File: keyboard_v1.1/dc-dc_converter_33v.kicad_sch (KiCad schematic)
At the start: 14 parts, among them Q2 AO3400A, U3 max1771esa+T

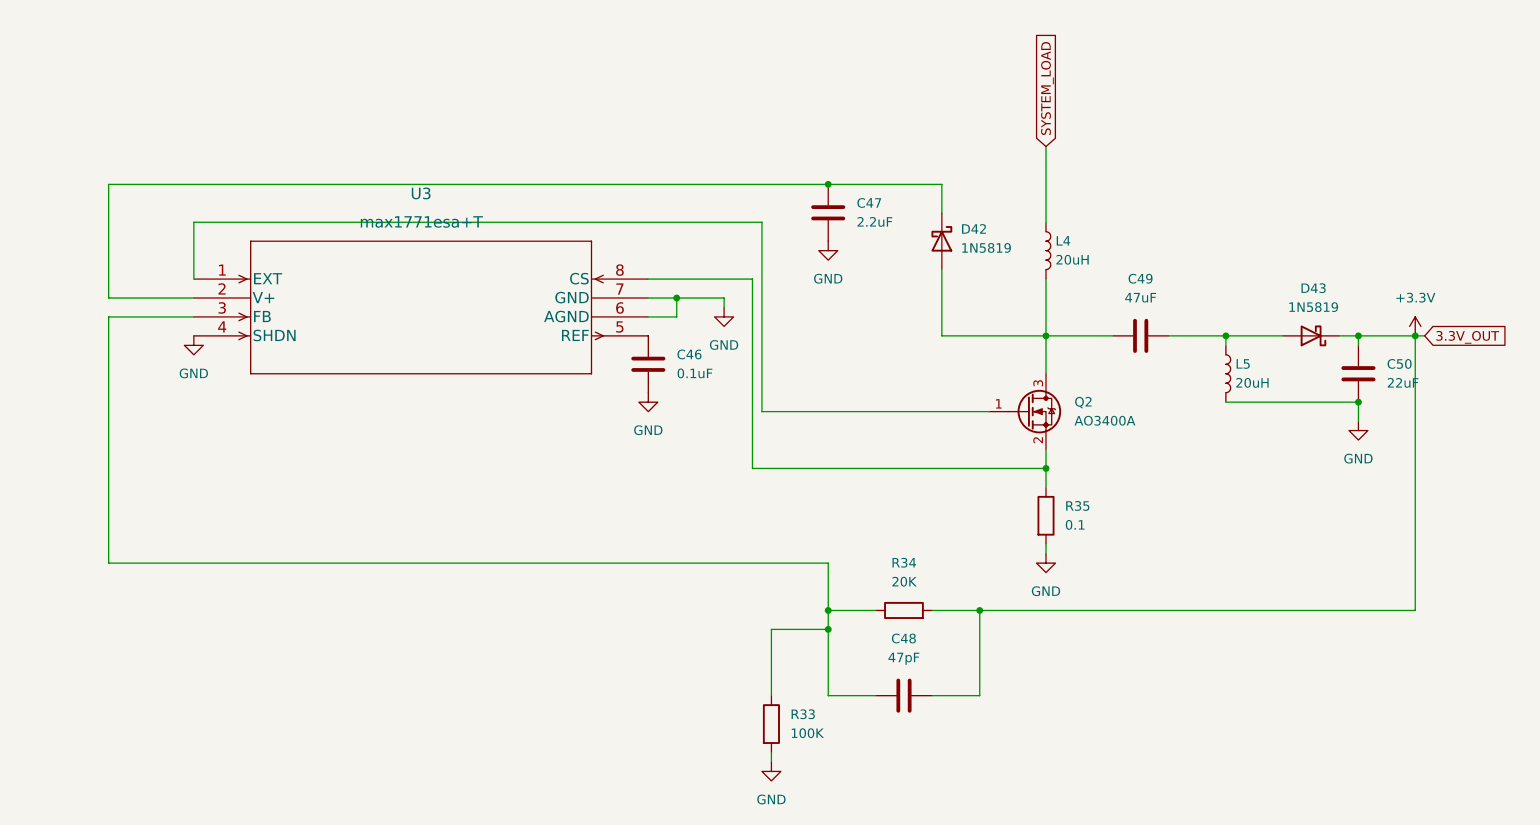
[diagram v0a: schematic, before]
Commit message: New design - schematics added (2022.07.20.)
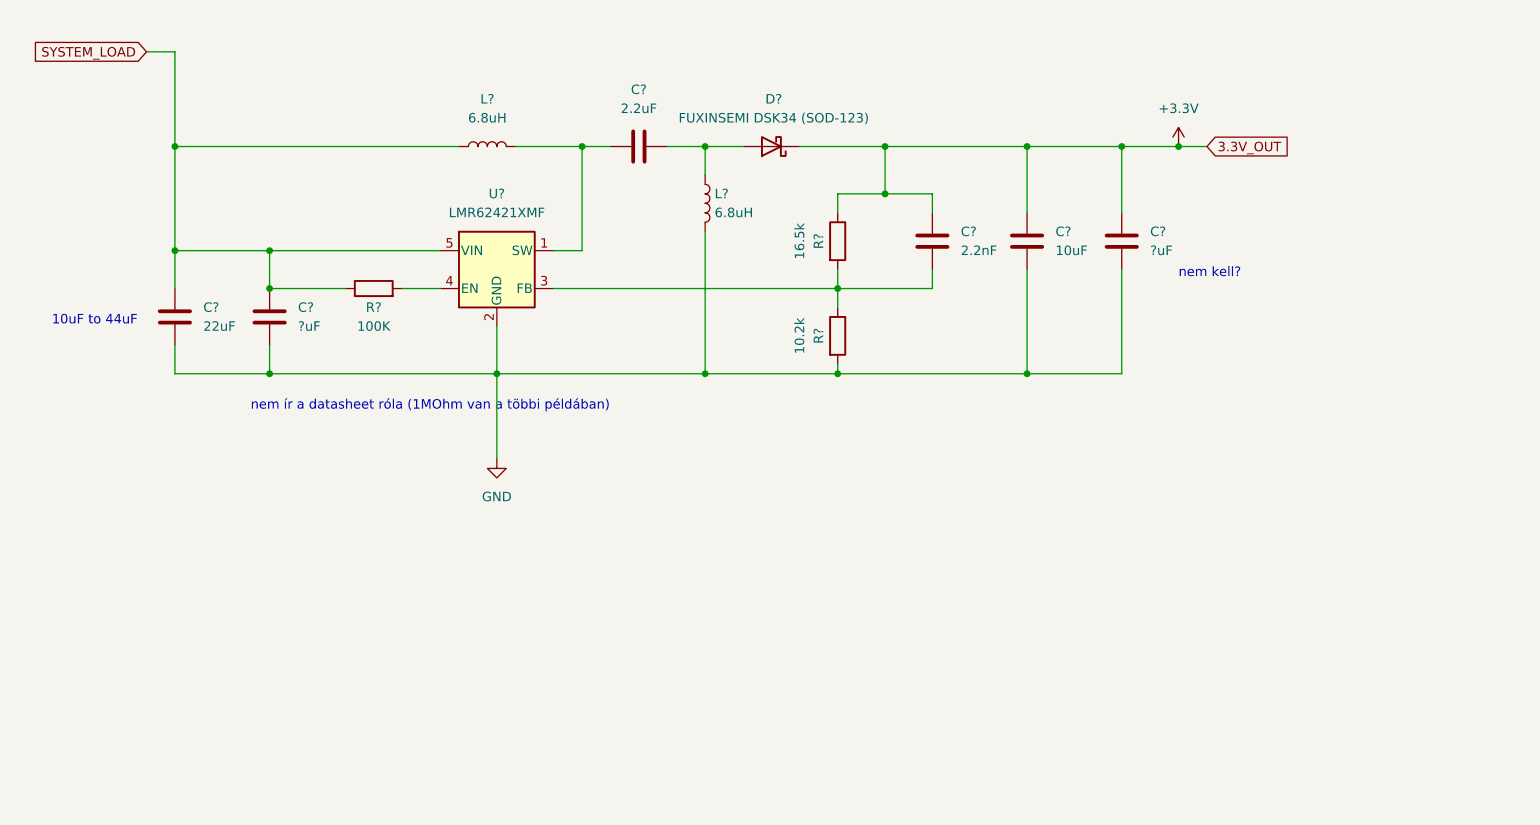
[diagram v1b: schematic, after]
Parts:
- removed C46: 0.1uF, Capacitor_SMD:C_0805_2012Metric_Pad1.18x1.45mm_HandSolder, symbol Device:C
- removed C47: 2.2uF, Capacitor_SMD:C_0805_2012Metric_Pad1.18x1.45mm_HandSolder, symbol Device:C
- removed C48: 47pF, Capacitor_SMD:C_0805_2012Metric_Pad1.18x1.45mm_HandSolder, symbol Device:C
- removed C49: 47uF, Capacitor_THT:CP_Radial_D4.0mm_P1.50mm, symbol Device:C
- removed C50: 22uF, Capacitor_SMD:C_0805_2012Metric_Pad1.18x1.45mm_HandSolder, symbol Device:C
- removed D42, D43: 1N5819, Diode_THT:D_DO-41_SOD81_P10.16mm_Horizontal, symbol Diode:1N5819
- removed L4, L5: 20uH, inductors:inductors, symbol Device:L
- removed Q2: AO3400A, Package_TO_SOT_SMD:SOT-23, symbol Transistor_FET:AO3400A
- removed R33: 100K, Resistor_SMD:R_0805_2012Metric_Pad1.20x1.40mm_HandSolder, symbol Device:R
- removed R34: 20K, Resistor_SMD:R_0805_2012Metric_Pad1.20x1.40mm_HandSolder, symbol Device:R
- removed R35: 0.1, Resistor_SMD:R_0805_2012Metric_Pad1.20x1.40mm_HandSolder, symbol Device:R
- removed U3: max1771esa+T, max1771:max1771esa&plus_T, symbol max1771:max1771esa+T
- added C?: 2.2nF, Capacitor_SMD:C_0805_2012Metric_Pad1.18x1.45mm_HandSolder, symbol Device:C
- added C? (x2): ?uF, Capacitor_SMD:C_0805_2012Metric_Pad1.18x1.45mm_HandSolder, symbol Device:C
- added C?: 22uF, Capacitor_SMD:C_0805_2012Metric_Pad1.18x1.45mm_HandSolder, symbol Device:C
- added C?: 10uF, Capacitor_SMD:C_0805_2012Metric_Pad1.18x1.45mm_HandSolder, symbol Device:C
- added C?: 2.2uF, Capacitor_SMD:C_0805_2012Metric_Pad1.18x1.45mm_HandSolder, symbol Device:C
- added D?: FUXINSEMI DSK34 (SOD-123), Diode_SMD:D_SOD-123, symbol Diode:BAT42W-V
- added L? (x2): 6.8uH, inductors:inductors, symbol Device:L
- added R?: 10.2k, Resistor_SMD:R_0805_2012Metric_Pad1.20x1.40mm_HandSolder, symbol Device:R
- added R?: 16.5k, Resistor_SMD:R_0805_2012Metric_Pad1.20x1.40mm_HandSolder, symbol Device:R
- added R?: 100K, Resistor_SMD:R_0805_2012Metric_Pad1.20x1.40mm_HandSolder, symbol Device:R
- added U?: LMR62421XMF, Package_TO_SOT_SMD:SOT-23-5, symbol Regulator_Switching:LMR62421XMF
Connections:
- net +3V3: now also C?.1, C?.1, C?.1, D?.1 (K), R?.1
- net GND: now also C?.2, C?.2, C?.2, C?.2, L?.2, R?.2, U?.2 (GND)
- net SYSTEM_LOAD: now also C?.1, C?.1, L?.1, R?.1, U?.5 (VIN)
- new net: C?.2, R?.1, R?.2, U?.3 (FB)
- new net: C?.2, D?.2 (A), L?.1
- new net: C?.1, L?.2, U?.1 (SW)
- new net: R?.2, U?.4 (EN)
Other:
- note added: "10uF to 44uF"
- note added: "nem kell?"
- note added: "nem ír a datasheet róla (1MOhm van a többi példában)"

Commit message: PCB layout done - 2022.07.25.
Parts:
- removed C?: ?uF, Capacitor_SMD:C_0805_2012Metric_Pad1.18x1.45mm_HandSolder, symbol Device:C
- L2, L3: renamed from L?; footprint inductors:inductors -> inductors:inductor_koherelec
- R18: renamed from R?; value 16.5k -> 9.1k
- R19: renamed from R?; value 10.2k -> 5.6k
- gave numbers to parts that had none: 8
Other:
- note removed: "nem ír a datasheet róla (1MOhm van a többi példában)"
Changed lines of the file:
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@@
   (junction (at 165.1 50.8) (diameter 0) (color 0 0 0 0)
   )
-  (junction (at 63.5 81.28) (diameter 0) (color 0 0 0 0)
-  )
   (junction (at 121.92 81.28) (diameter 0) (color 0 0 0 0)
   )
   (junction (at 146.05 50.8) (diameter 0) (color 0 0 0 0)
   )
-  (junction (at 63.5 69.85) (diameter 0) (color 0 0 0 0)
-  )
   (junction (at 139.7 69.85) (diameter 0) (color 0 0 0 0)
   )
@@
     (stroke (width 0) (type default) (color 0 0 0 0))
   )
-  (wire (pts (xy 50.8 81.28) (xy 63.5 81.28))
-    (stroke (width 0) (type default) (color 0 0 0 0))
-  )
   (wire (pts (xy 63.5 69.85) (xy 73.66 69.85))
     (stroke (width 0) (type default) (color 0 0 0 0))
@@
     (stroke (width 0) (type default) (color 0 0 0 0))
   )
-  (wire (pts (xy 63.5 77.47) (xy 63.5 81.28))
-    (stroke (width 0) (type default) (color 0 0 0 0))
-  )
   (wire (pts (xy 93.98 81.28) (xy 93.98 92.71))
     (stroke (width 0) (type default) (color 0 0 0 0))
@@
     (stroke (width 0) (type default) (color 0 0 0 0))
   )
-  (wire (pts (xy 63.5 81.28) (xy 93.98 81.28))
+  (wire (pts (xy 50.8 81.28) (xy 93.98 81.28))
     (stroke (width 0) (type default) (color 0 0 0 0))
   )
@@
   )
   (text "10uF to 44uF" (at 34.29 74.93 0)
-    (effects (font (size 1.27 1.27)) (justify left bottom))
-  )
-  (text "nem ír a datasheet róla (1MOhm van a többi példában)"
-    (at 60.96 86.36 0)
     (effects (font (size 1.27 1.27)) (justify left bottom))
   )
@@
   (symbol (lib_id "Device:C") (at 152.4 63.5 0) (unit 1)
     (in_bom yes) (on_board yes) (fields_autoplaced)
-    (property "Reference" "C?" (id 0) (at 156.21 62.2299 0)
+    (property "Reference" "C22" (id 0) (at 156.21 62.2299 0)
       (effects (font (size 1.27 1.27)) (justify left))
     )
@@
   (symbol (lib_id "Device:R") (at 139.7 76.2 0) (unit 1)
     (in_bom yes) (on_board yes)
-    (property "Reference" "R?" (id 0) (at 137.16 76.2 90))
-    (property "Value" "10.2k" (id 1) (at 134.62 76.2 90))
+    (property "Reference" "R19" (id 0) (at 137.16 76.2 90))
+    (property "Value" "5.6k" (id 1) (at 134.62 76.2 90))
     (property "Footprint" "Resistor_SMD:R_0805_2012Metric_Pad1.20x1.40mm_HandSolder" (id 2) (at 137.922 76.2 90)
       (effects (font (size 1.27 1.27)) hide)
@@
   (symbol (lib_id "Device:C") (at 177.8 63.5 0) (unit 1)
     (in_bom yes) (on_board yes) (fields_autoplaced)
-    (property "Reference" "C?" (id 0) (at 181.61 62.2299 0)
+    (property "Reference" "C24" (id 0) (at 181.61 62.2299 0)
       (effects (font (size 1.27 1.27)) (justify left))
     )
@@
   (symbol (lib_id "Device:C") (at 50.8 73.66 0) (unit 1)
     (in_bom yes) (on_board yes) (fields_autoplaced)
-    (property "Reference" "C?" (id 0) (at 54.61 72.3899 0)
+    (property "Reference" "C17" (id 0) (at 54.61 72.3899 0)
       (effects (font (size 1.27 1.27)) (justify left))
     )
@@
   (symbol (lib_id "power:GND") (at 93.98 92.71 0) (unit 1)
     (in_bom yes) (on_board yes) (fields_autoplaced)
-    (property "Reference" "#PWR?" (id 0) (at 93.98 99.06 0)
+    (property "Reference" "#PWR0144" (id 0) (at 93.98 99.06 0)
       (effects (font (size 1.27 1.27)) hide)
     )
@@
   (symbol (lib_id "Diode:BAT42W-V") (at 130.81 50.8 180) (unit 1)
     (in_bom yes) (on_board yes) (fields_autoplaced)
-    (property "Reference" "D?" (id 0) (at 131.1275 44.45 0))
+    (property "Reference" "D14" (id 0) (at 131.1275 44.45 0))
     (property "Value" "FUXINSEMI DSK34 (SOD-123)" (id 1) (at 131.1275 46.99 0))
     (property "Footprint" "Diode_SMD:D_SOD-123" (id 2) (at 130.81 46.355 0)
@@
     (pin "2")
   )
-  (symbol (lib_id "Device:C") (at 63.5 73.66 0) (unit 1)
-    (in_bom yes) (on_board yes) (fields_autoplaced)
-    (property "Reference" "C?" (id 0) (at 67.31 72.3899 0)
-      (effects (font (size 1.27 1.27)) (justify left))
-    )
-    (property "Value" "?uF" (id 1) (at 67.31 74.9299 0)
-      (effects (font (size 1.27 1.27)) (justify left))
-    )
-    (property "Footprint" "Capacitor_SMD:C_0805_2012Metric_Pad1.18x1.45mm_HandSolder" (id 2) (at 64.4652 77.47 0)
-      (effects (font (size 1.27 1.27)) hide)
-    )
-    (property "Datasheet" "~" (id 3) (at 63.5 73.66 0)
-      (effects (font (size 1.27 1.27)) hide)
-    )
-    (pin "1")
-    (pin "2")
-  )
   (symbol (lib_id "power:+3.3V") (at 185.42 50.8 0) (unit 1)
     (in_bom yes) (on_board yes) (fields_autoplaced)
-    (property "Reference" "#PWR?" (id 0) (at 185.42 54.61 0)
+    (property "Reference" "#PWR0145" (id 0) (at 185.42 54.61 0)
       (effects (font (size 1.27 1.27)) hide)
     )
@@
   (symbol (lib_id "Device:C") (at 165.1 63.5 0) (unit 1)
     (in_bom yes) (on_board yes) (fields_autoplaced)
-    (property "Reference" "C?" (id 0) (at 168.91 62.2299 0)
+    (property "Reference" "C23" (id 0) (at 168.91 62.2299 0)
       (effects (font (size 1.27 1.27)) (justify left))
     )
@@
   (symbol (lib_id "Device:C") (at 113.03 50.8 90) (unit 1)
     (in_bom yes) (on_board yes) (fields_autoplaced)
-    (property "Reference" "C?" (id 0) (at 113.03 43.18 90))
+    (property "Reference" "C18" (id 0) (at 113.03 43.18 90))
     (property "Value" "2.2uF" (id 1) (at 113.03 45.72 90))
     (property "Footprint" "Capacitor_SMD:C_0805_2012Metric_Pad1.18x1.45mm_HandSolder" (id 2) (at 116.84 49.8348 0)
@@
   (symbol (lib_id "Regulator_Switching:LMR62421XMF") (at 93.98 67.31 0) (unit 1)
     (in_bom yes) (on_board yes) (fields_autoplaced)
-    (property "Reference" "U?" (id 0) (at 93.98 57.15 0))
+    (property "Reference" "U1" (id 0) (at 93.98 57.15 0))
     (property "Value" "LMR62421XMF" (id 1) (at 93.98 59.69 0))
     (property "Footprint" "Package_TO_SOT_SMD:SOT-23-5" (id 2) (at 95.25 73.66 0)
@@
   (symbol (lib_id "Device:R") (at 139.7 63.5 0) (unit 1)
     (in_bom yes) (on_board yes)
-    (property "Reference" "R?" (id 0) (at 137.16 63.5 90))
-    (property "Value" "16.5k" (id 1) (at 134.62 63.5 90))
+    (property "Reference" "R18" (id 0) (at 137.16 63.5 90))
+    (property "Value" "9.1k" (id 1) (at 134.62 63.5 90))
     (property "Footprint" "Resistor_SMD:R_0805_2012Metric_Pad1.20x1.40mm_HandSolder" (id 2) (at 137.922 63.5 90)
       (effects (font (size 1.27 1.27)) hide)
@@
   (symbol (lib_id "Device:L") (at 92.71 50.8 90) (unit 1)
     (in_bom yes) (on_board yes) (fields_autoplaced)
-    (property "Reference" "L?" (id 0) (at 92.71 44.45 90))
+    (property "Reference" "L2" (id 0) (at 92.71 44.45 90))
     (property "Value" "6.8uH" (id 1) (at 92.71 46.99 90))
-    (property "Footprint" "inductors:inductors" (id 2) (at 92.71 50.8 0)
+    (property "Footprint" "inductors:inductor_koherelec" (id 2) (at 92.71 50.8 0)
       (effects (font (size 1.27 1.27)) hide)
     )
@@
   (symbol (lib_id "Device:R") (at 77.47 69.85 90) (unit 1)
     (in_bom yes) (on_board yes)
-    (property "Reference" "R?" (id 0) (at 77.47 72.39 90))
+    (property "Reference" "R17" (id 0) (at 77.47 72.39 90))
     (property "Value" "100K" (id 1) (at 77.47 74.93 90))
     (property "Footprint" "Resistor_SMD:R_0805_2012Metric_Pad1.20x1.40mm_HandSolder" (id 2) (at 77.47 71.628 90)
@@
   (symbol (lib_id "Device:L") (at 121.92 58.42 0) (unit 1)
     (in_bom yes) (on_board yes) (fields_autoplaced)
-    (property "Reference" "L?" (id 0) (at 123.19 57.1499 0)
+    (property "Reference" "L3" (id 0) (at 123.19 57.1499 0)
       (effects (font (size 1.27 1.27)) (justify left))
     )
@@
       (effects (font (size 1.27 1.27)) (justify left))
     )
-    (property "Footprint" "inductors:inductors" (id 2) (at 121.92 58.42 0)
-      (effects (font (size 1.27 1.27)) hide)
-    )
+    (property "Footprint" "inductors:inductor_koherelec" (id 2) (at 121.92 58.42 0)
+      (effects (font (size 1.27 1.27)) hide)
+    )
